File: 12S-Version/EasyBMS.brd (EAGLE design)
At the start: 49 x 100 mm, 148 parts, among them J1 SSM-120-SM-DV, Q10 BSS84LT1G, Q11 BSS84LT1G, Q12 BSS84LT1G, Q13 BSS84LT1G, Q2 BSS84LT1G, Q3 BSS84LT1G, Q4 BSS84LT1G, Q5 BSS84LT1G, Q6 BSS84LT1G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

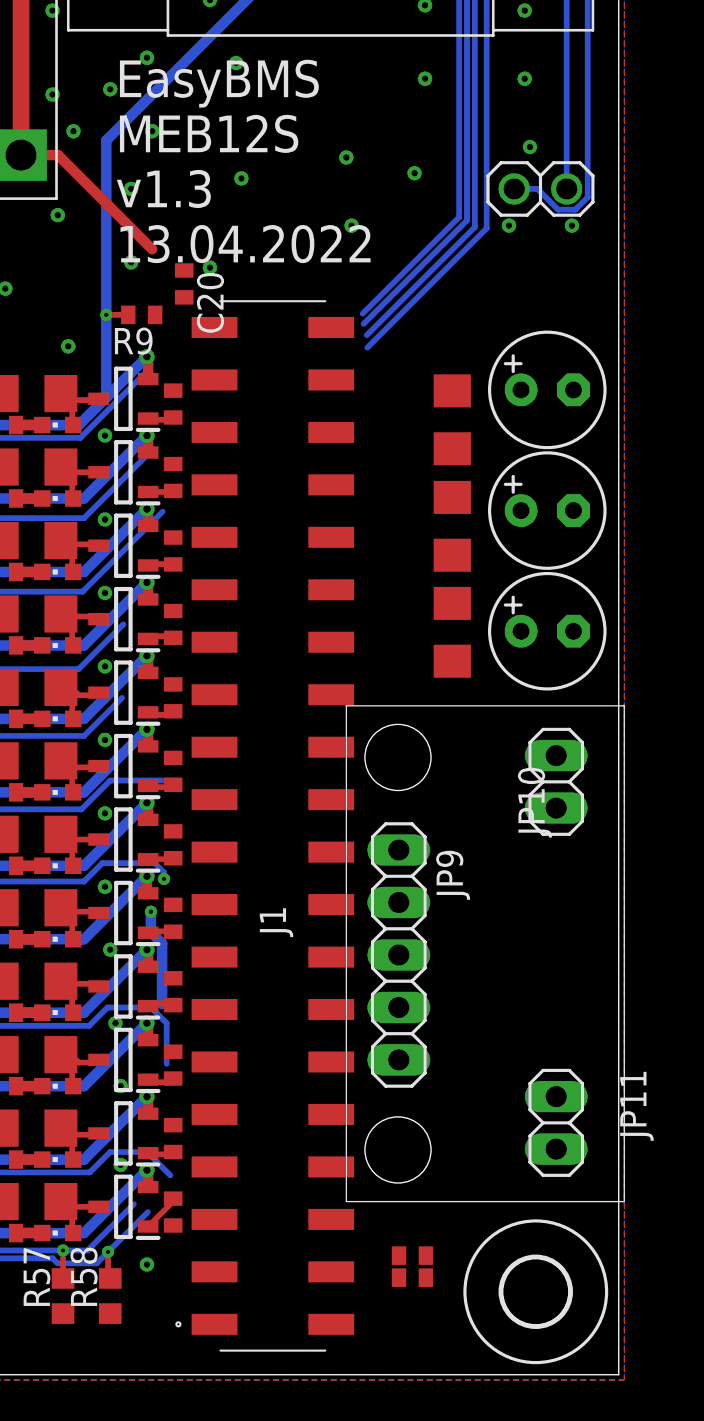
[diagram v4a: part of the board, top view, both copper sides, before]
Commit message: IC directly placed on base board, no tracing done
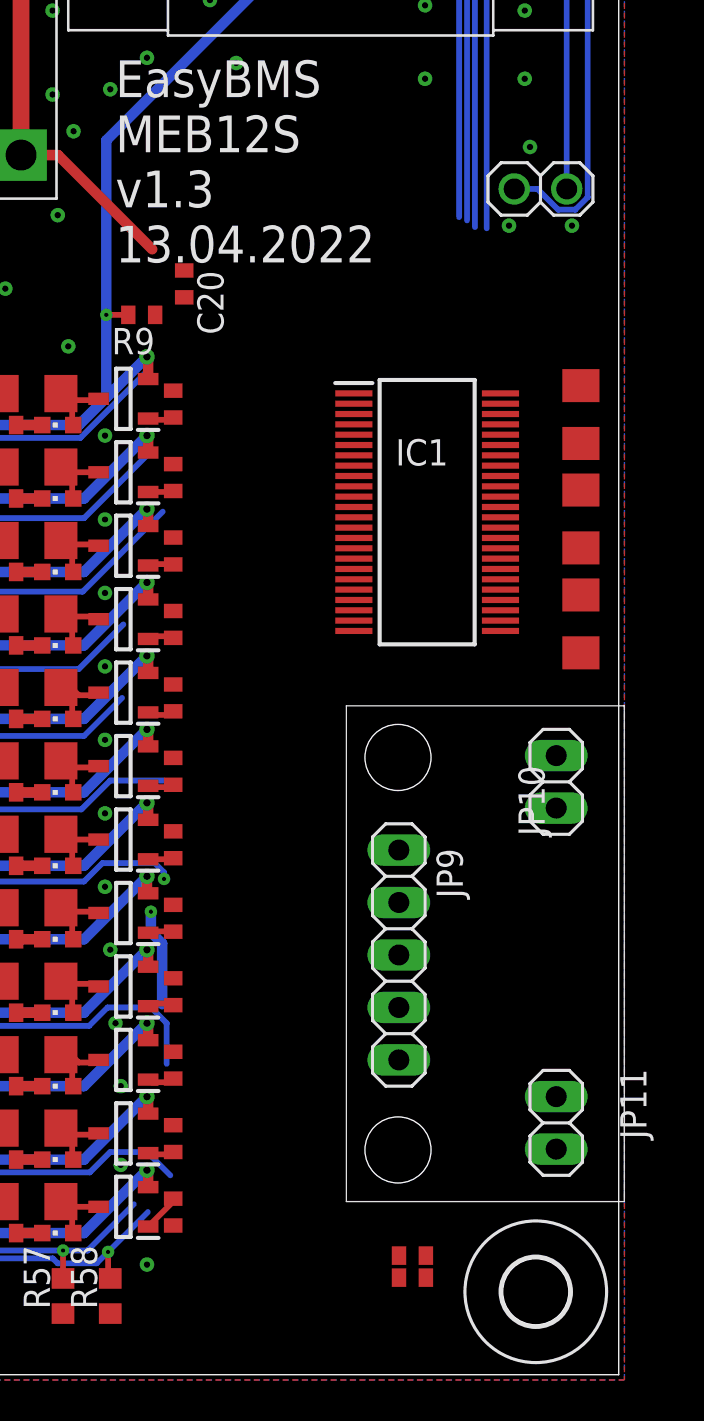
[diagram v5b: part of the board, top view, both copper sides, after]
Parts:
- removed C18: 100nF, rcl:C1206
- removed C2, C3: 1uF, rcl:E2,5-6
- removed J1: SSM-120-SM-DV, SamacSys_Parts:SSM-120-XXX-DV
- added IC1: LTC6811IG-2#PBF, SamacSys_Parts:SOP50P780X200-48N
- C1: device rcl:E2,5-6 -> rcl:C1206
- C19, C4: value 100nF -> 1uF
- moved C4 6.24 mm to (47.2, 36.3)
- moved C19 6.23 mm to (47.2, 46.5)
- moved C1 1.68 mm to (47.2, 41.4), turned to 270 degrees
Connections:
- net 5VDC: now also IC1.36, IC1.37; no longer C3.+, J1.32
- net C0: now also IC1.26; no longer J1.12
- net C1: now also IC1.24; no longer J1.8
- net C10: now also IC1.6; no longer J1.29
- net C11: now also IC1.4; no longer J1.33
- net C12: now also IC1.2; no longer J1.37
- net C2: now also IC1.22; no longer J1.4
- net C3: now also IC1.20; no longer J1.1
- net C4: now also IC1.18; no longer J1.5
- net C5: now also IC1.16; no longer J1.9
- net C6: now also IC1.14; no longer J1.13
- net C7: now also IC1.12; no longer J1.17
- net C8: now also IC1.10; no longer J1.21
- net C9: now also IC1.8; no longer J1.25
- net CSB: now also IC1.41; no longer J1.34
- net GND: now also C1.2, IC1.30, IC1.31, IC1.40, IC1.45, IC1.46, IC1.47, IC1.48; no longer C1.-, C18.2, C2.-, C3.-, J1.24, J1.26
- net GPIO4: now also IC1.32; no longer J1.20
- net GPIO5: now also IC1.33; no longer J1.22
- net ISIGNAL: now also IC1.29; no longer J1.18
- net MISO: now also IC1.44; no longer J1.40
- net MOSI: now also IC1.43; no longer J1.38
- net S1: now also IC1.25; no longer J1.10
- net S10: now also IC1.7; no longer J1.27
- net S11: now also IC1.5; no longer J1.31
- net S12: now also IC1.3; no longer J1.35
- net S2: now also IC1.23; no longer J1.6
- net S3: now also IC1.21; no longer J1.2
- net S4: now also IC1.19; no longer J1.3
- net S5: now also IC1.17; no longer J1.7
- net S6: now also IC1.15; no longer J1.11
- net S7: now also IC1.13; no longer J1.15
- net S8: now also IC1.11; no longer J1.19
- net S9: now also IC1.9; no longer J1.23
- net SCK: now also IC1.42; no longer J1.36
- net V+: now also IC1.1; no longer J1.39
- net VREF1: now also C1.1, IC1.35; no longer C1.+, C18.1, J1.30
- net VREF2: now also IC1.34; no longer C2.+, J1.28
- net VTEMP1: now also IC1.27; no longer J1.14
- net VTEMP2: now also IC1.28; no longer J1.16
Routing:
- net SCK: track 29.0 -> 20.9 mm
- net MOSI: track 36.4 -> 29.0 mm
- net CSB: track 36.3 -> 29.2 mm
- net MISO: track 32.7 -> 26.1 mm
- net GND: vias 118 -> 110

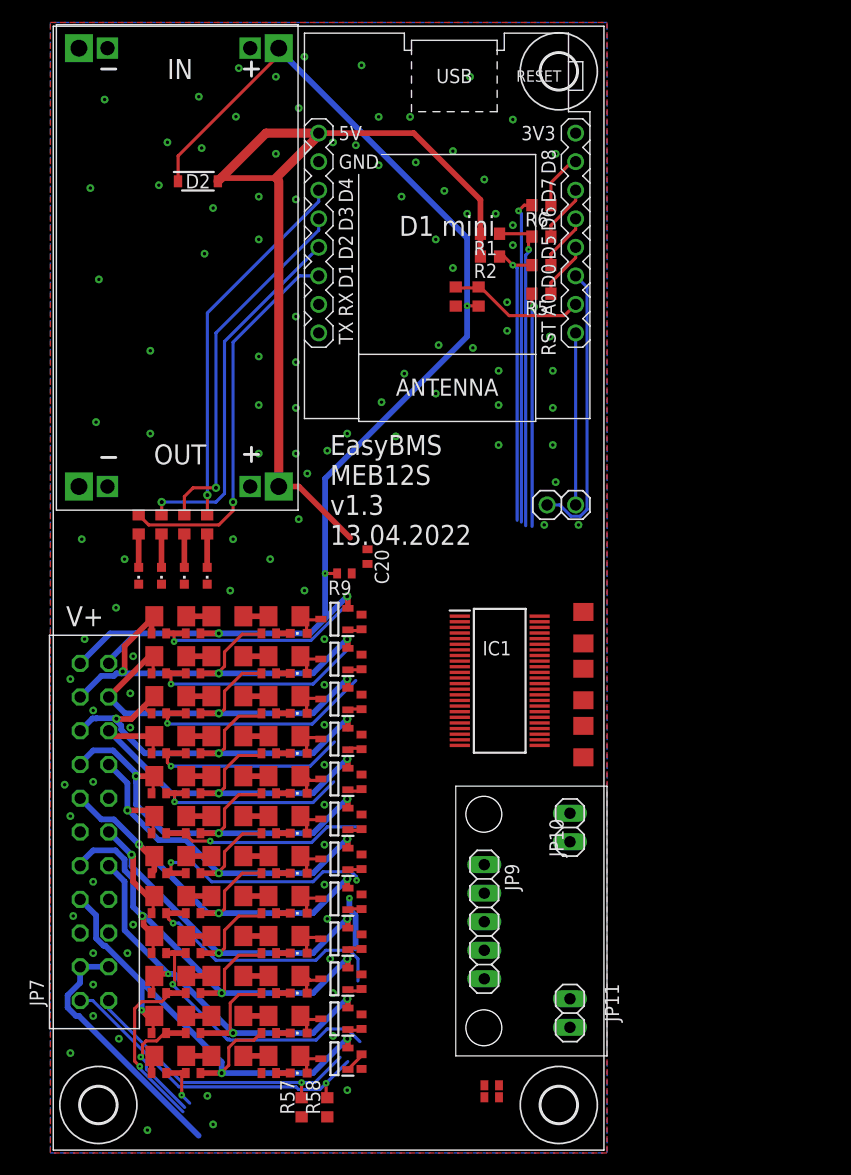
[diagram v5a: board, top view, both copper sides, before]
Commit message: Routing nearly done, difficult lines done
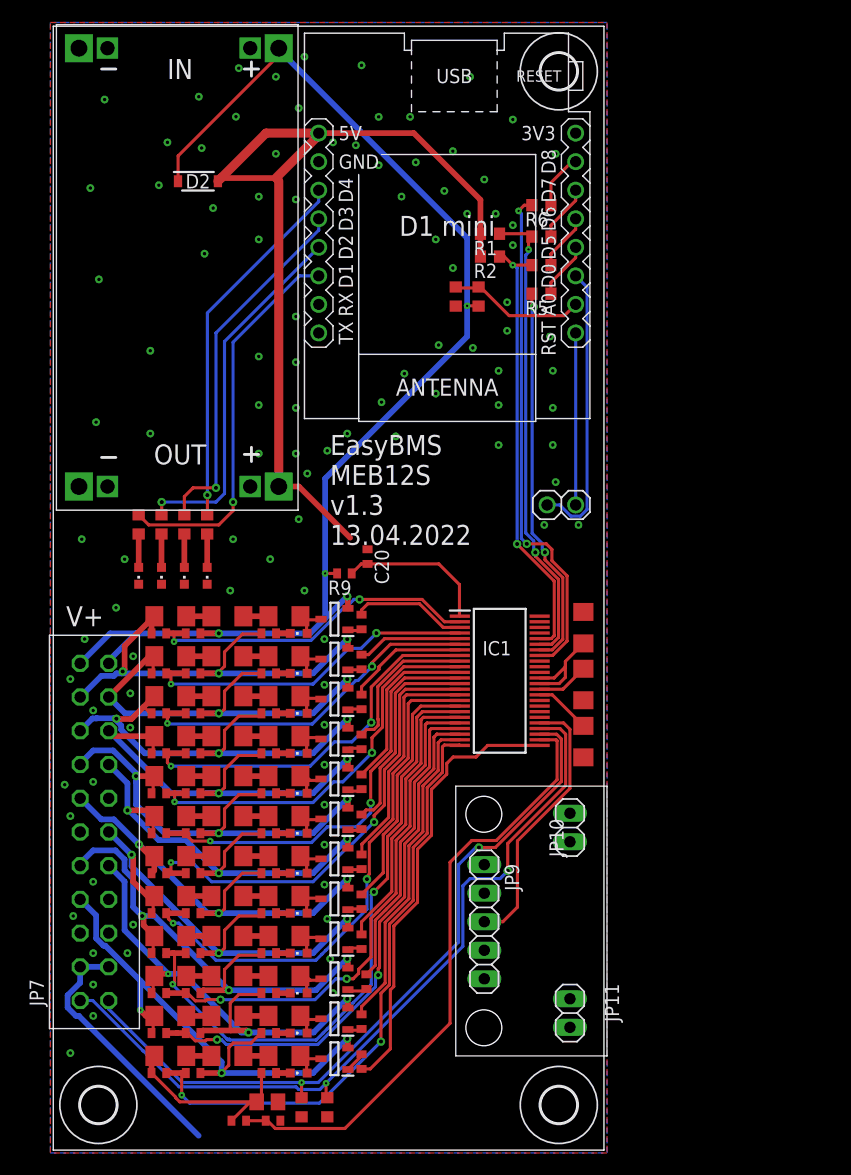
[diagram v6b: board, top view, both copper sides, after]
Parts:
- added R13: C1017, rcl:R0805
- moved R3 22.7 mm to (16.5, 2.62), turned to 180 degrees
- moved C5 19.6 mm to (19.6, 2.62)
- moved R34 0.43 mm to (27.9, 15.0)
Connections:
- new net C1-: C6.2, R11.2, R13.1, R3.2, R4.1
- net GND: now also R13.2; no longer C6.2, R11.2, R3.2, R4.1
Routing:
- net C0: track 0.64 -> 54.3 mm
- net C1: track 4.72 -> 54.1 mm, vias 1 -> 2
- net VTEMP2: track 29.5 -> 70.7 mm, vias 1 -> 2
- net VTEMP1: track 26.3 -> 66.1 mm, vias 1 -> 2
- net S1: track 0.00 -> 39.7 mm
- net C2: track 11.5 -> 48.8 mm, vias 1 -> 2
- net C4: track 24.9 -> 56.6 mm, vias 1 -> 2
- net C3: track 16.4 -> 47.9 mm, vias 1 -> 2
- net S2: track 0.00 -> 29.0 mm
- net S3: track 0.00 -> 26.8 mm
- net S4: track 0.00 -> 24.8 mm
- net C5: track 23.3 -> 47.9 mm, vias 1 -> 2
- net ISIGNAL: track 0.00 -> 24.2 mm
- net C6: track 20.8 -> 41.5 mm
- net S6: track 0.05 -> 20.6 mm
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
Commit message: everything routed, no DRC errors
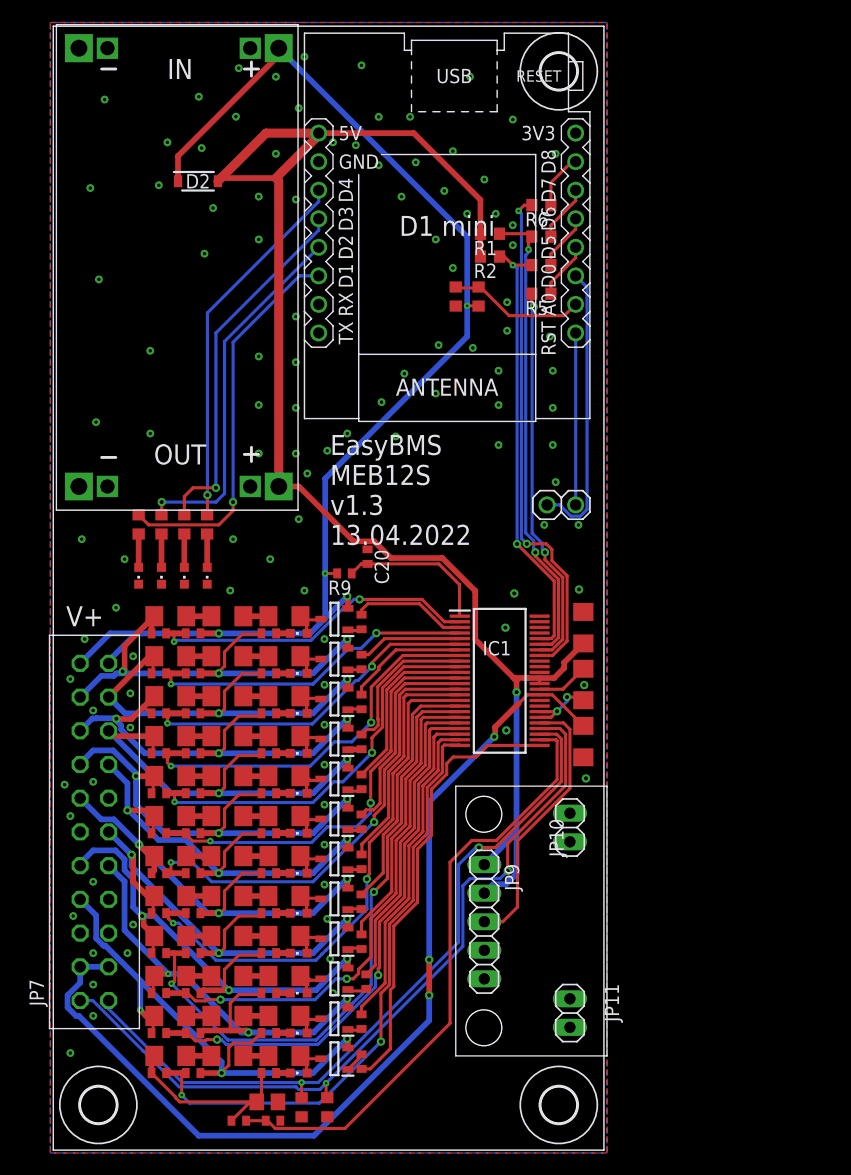
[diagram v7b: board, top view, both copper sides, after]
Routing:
- net VREF2: track 28.3 -> 86.5 mm, vias 0 -> 3
- net 5VDC: track 88.1 -> 138.6 mm, vias 0 -> 1
- net GND: track 0.36 -> 6.86 mm, vias 104 -> 112
- net C4: track 56.6 -> 56.1 mm

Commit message: cosmetics
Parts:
- removed D2: SM4007PL-TP, SamacSys_Parts:SODFL3616X135N
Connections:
- net 5VDC: no longer D2.2
- net C12+: no longer D2.1
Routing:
- net 5VDC: track 138.6 -> 122.5 mm
- net C12+: track 113.2 -> 97.7 mm
- net GND: vias 112 -> 128
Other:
- board text added: "EasyBMS MEB12S v1.4 19.07.2022"
- board text removed: "EasyBMS MEB12S v1.3 13.04.2022"
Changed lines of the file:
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@@
 <text x="24.638" y="53.848" size="1.778" layer="25">EasyBMS
 MEB12S
-v1.3
-13.04.2022</text>
+v1.4
+19.07.2022</text>
 </plain>
 <attributes>
@@
 <attribute name="VALUE" x="18.923" y="0.7112" size="1.27" layer="27"/>
 </element>
-<element name="D2" library="SamacSys_Parts" package="SODFL3616X135N" value="SM4007PL-TP" x="12.876" y="86.203" smashed="yes">
-<attribute name="DESCRIPTION" value="Rectifiers 1A, 1000V 1A, 1000V" x="12.876" y="86.203" size="1.778" layer="27" display="off"/>
-<attribute name="HEIGHT" value="1.35mm" x="12.876" y="86.203" size="1.778" layer="27" display="off"/>
-<attribute name="MANUFACTURER_NAME" value="Micro Commercial Components (MCC)" x="12.876" y="86.203" size="1.778" layer="27" display="off"/>
-<attribute name="MANUFACTURER_PART_NUMBER" value="SM4007PL-TP" x="12.876" y="86.203" size="1.778" layer="27" display="off"/>
-<attribute name="MOUSER_PART_NUMBER" value="833-SM4007PL-TP" x="12.876" y="86.203" size="1.778" layer="27" display="off"/>
-<attribute name="MOUSER_PRICE-STOCK" value="https://www.mouser.co.uk/ProductDetail/Micro-Commercial-Components-MCC/SM4007PL-TP?qs=SdqRYZZ9IxCh9ylwm1K3UA%3D%3D" x="12.876" y="86.203" size="1.778" layer="27" display="off"/>
-<attribute name="NAME" x="12.876" y="86.203" size="1.27" layer="25" align="center"/>
-</element>
 <element name="R14" library="rcl" library_urn="urn:adsk.eagle:library:334" package="R1206" package3d_urn="urn:adsk.eagle:package:23540/2" value="10R0" x="10.414" y="11.938" smashed="yes"/>
 <element name="R20" library="rcl" library_urn="urn:adsk.eagle:library:334" package="R1206" package3d_urn="urn:adsk.eagle:package:23540/2" value="10R0" x="15.494" y="11.938" smashed="yes"/>
@@
 </element>
 <element name="JP11" library="pinhead" library_urn="urn:adsk.eagle:library:325" package="1X02" package3d_urn="urn:adsk.eagle:package:22435/2" value="" x="45.974" y="12.192" smashed="yes" rot="R270">
-<attribute name="NAME" x="49.0728" y="14.8082" size="1.27" layer="25" ratio="10" rot="R270"/>
 <attribute name="VALUE" x="44.069" y="14.732" size="1.27" layer="27" rot="R270"/>
 </element>
@@
 </element>
 <element name="JP7" library="pinhead_own" package="2X11_MEB12S" value="" x="3.666" y="28.308" smashed="yes" rot="R90">
-<attribute name="NAME" x="-0.834" y="12.808" size="1.27" layer="25" ratio="10" rot="R90"/>
 <attribute name="VALUE" x="9.166" y="12.808" size="1.27" layer="27" rot="R90"/>
 </element>
@@
 <contactref element="R2" pad="2"/>
 <contactref element="U$2" pad="JP2.8"/>
-<contactref element="D2" pad="2"/>
 <contactref element="R1" pad="2"/>
 <contactref element="C19" pad="1"/>
 <contactref element="JP9" pad="1"/>
 <contactref element="JP9" pad="2"/>
-<wire x1="14.935" y1="86.487" x2="19.812" y2="86.487" width="0.508" layer="1"/>
 <wire x1="23.622" y1="90.487" x2="32.07810625" y2="90.487" width="0.508" layer="1"/>
 <wire x1="38.012" y1="79.502" x2="38.012" y2="81.534" width="0.508" layer="1"/>
-<wire x1="20.066" y1="86.233" x2="20.066" y2="59.044" width="0.8128" layer="1"/>
-<wire x1="23.812" y1="90.487" x2="19.812" y2="86.487" width="0.8128" layer="1"/>
-<wire x1="23.812" y1="90.487" x2="23.622" y2="90.487" width="0.8128" layer="1"/>
-<wire x1="14.651" y1="86.203" x2="14.935" y2="86.487" width="0.8128" layer="1"/>
-<wire x1="14.935" y1="86.487" x2="18.935" y2="90.487" width="0.8128" layer="1"/>
-<wire x1="18.935" y1="90.487" x2="23.622" y2="90.487" width="0.8128" layer="1"/>
 <wire x1="32.07810625" y1="90.487" x2="38.012" y2="84.55310625" width="0.508" layer="1"/>
 <wire x1="38.012" y1="84.55310625" x2="38.012" y2="81.534" width="0.508" layer="1"/>
 <wire x1="20.066" y1="59.044" x2="21.855" y2="59.044" width="0.508" layer="1"/>
-<wire x1="19.812" y1="86.487" x2="20.066" y2="86.233" width="0.508" layer="1"/>
 <contactref element="IC1" pad="37"/>
 <contactref element="IC1" pad="36"/>
@@
 <wire x1="41.2242" y1="41.7576" x2="40.9742" y2="42.0076" width="0.508" layer="1"/>
 <wire x1="41.2242" y1="28.2702" x2="41.2242" y2="40.7416" width="0.508" layer="16"/>
+<wire x1="20.066" y1="86.931" x2="23.622" y2="90.487" width="0.8128" layer="1"/>
+<wire x1="20.066" y1="59.044" x2="20.066" y2="86.931" width="0.8128" layer="1"/>
 </signal>
 <signal name="MISO">
@@
 <via x="46.7868" y="49.8856" extent="1-16" drill="0.35"/>
 <via x="47.244" y="41.3766" extent="1-16" drill="0.35"/>
+<via x="39.0144" y="33.2232" extent="1-16" drill="0.35"/>
+<via x="42.0116" y="16.9164" extent="1-16" drill="0.35"/>
+<via x="45.6438" y="20.9804" extent="1-16" drill="0.35"/>
+<via x="36.703" y="4.7752" extent="1-16" drill="0.35"/>
+<via x="32.1818" y="3.0734" extent="1-16" drill="0.35"/>
+<via x="37.4396" y="1.7526" extent="1-16" drill="0.35"/>
+<via x="35.3314" y="7.62" extent="1-16" drill="0.35"/>
+<via x="31.369" y="18.161" extent="1-16" drill="0.35"/>
+<via x="35.306" y="28.575" extent="1-16" drill="0.35"/>
+<via x="38.6334" y="39.1922" extent="1-16" drill="0.35"/>
+<via x="38.481" y="41.1988" extent="1-16" drill="0.35"/>
+<via x="39.7002" y="40.0812" extent="1-16" drill="0.35"/>
+<via x="38.481" y="42.9514" extent="1-16" drill="0.35"/>
+<via x="38.8112" y="47.1932" extent="1-16" drill="0.35"/>
+<via x="40.8178" y="44.8056" extent="1-16" drill="0.35"/>
+<via x="38.7604" y="56.9722" extent="1-16" drill="0.35"/>
 </signal>
 <signal name="N$202">
@@
 <contactref element="JP7" pad="1_TOTAL+"/>
 <contactref element="U$1" pad="IN+"/>
-<contactref element="D2" pad="1"/>
 <wire x1="5.062" y1="45.974" x2="7.366" y2="45.974" width="0.508" layer="16"/>
 <wire x1="14.732" y1="45.974" x2="7.366" y2="45.974" width="0.508" layer="16"/>
@@
 <wire x1="36.83" y1="72.39" x2="24.1935" y2="59.7535" width="0.508" layer="16"/>
 <wire x1="24.1935" y1="51.308" x2="24.1935" y2="47.3075" width="0.508" layer="16"/>
-<wire x1="11.101" y1="86.203" x2="11.101" y2="88.444" width="0.508" layer="1"/>
-<wire x1="20.066" y1="97.409" x2="20.066" y2="98.044" width="0.508" layer="1"/>
-<wire x1="11.101" y1="88.444" x2="20.066" y2="97.409" width="0.508" layer="1"/>
 <wire x1="20.066" y1="98.044" x2="36.83" y2="81.28" width="0.508" layer="16"/>
 <wire x1="36.83" y1="81.28" x2="36.83" y2="75.1205" width="0.508" layer="16"/>
